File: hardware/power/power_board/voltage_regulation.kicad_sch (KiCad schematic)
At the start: 14 parts, among them U601 TLV76733DRVx, U602 TLV76750DRVx

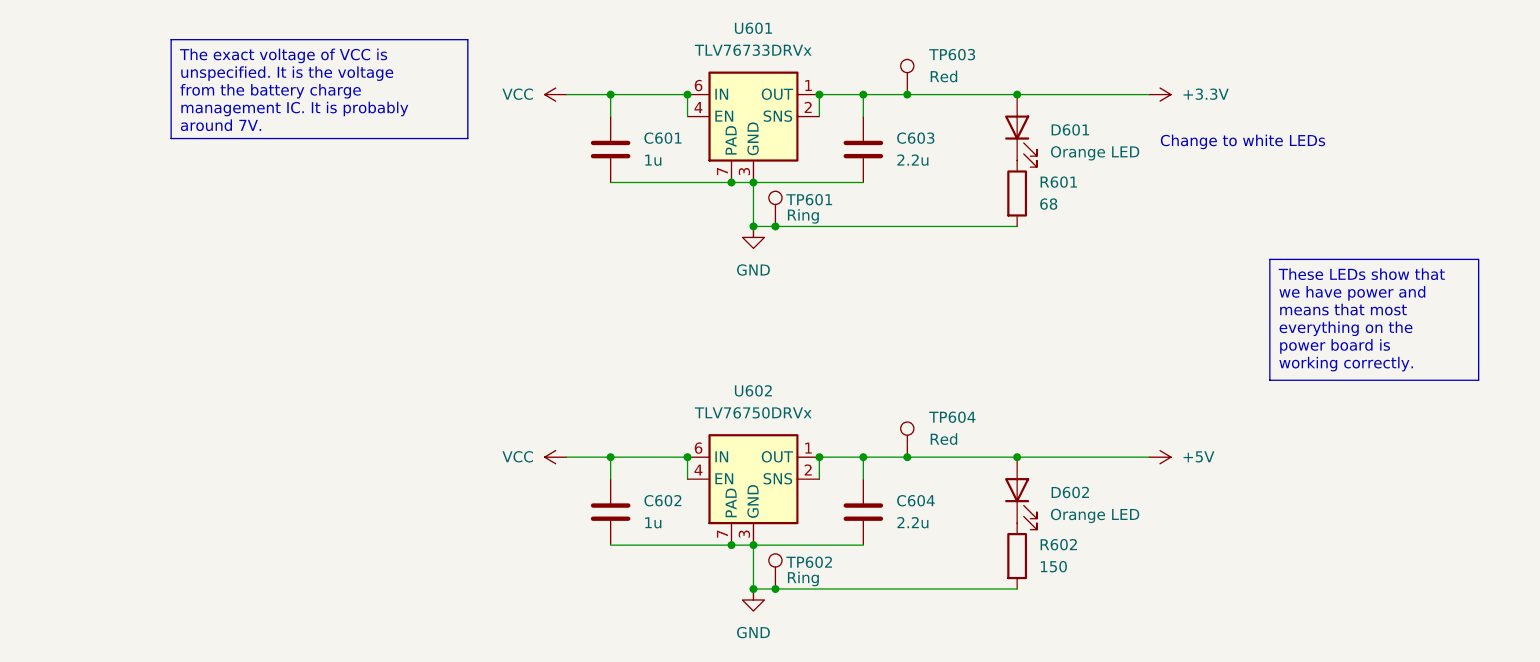
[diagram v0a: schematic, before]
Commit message: Changed interconnect from battery to power board to use the 10-pin Pico-Lock receptacle and cable.
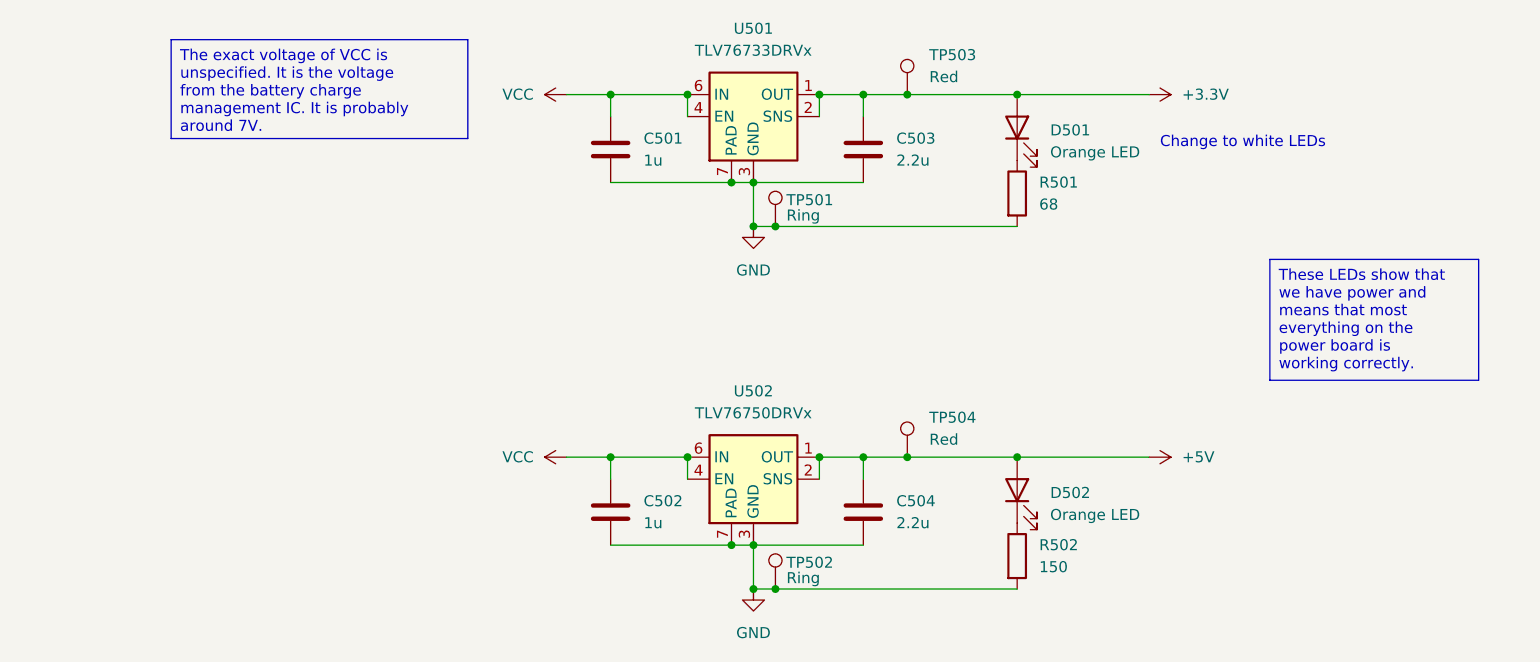
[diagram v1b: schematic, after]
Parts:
- renumbered C601 to C501, C602 to C502, C603 to C503, C604 to C504, D601 to D501, D602 to D502, R601 to R501, R602 to R502, TP601 to TP501, TP602 to TP502, TP603 to TP503, TP604 to TP504, U601 to U501, U602 to U502

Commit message: Checkpointing work on laying out the power board
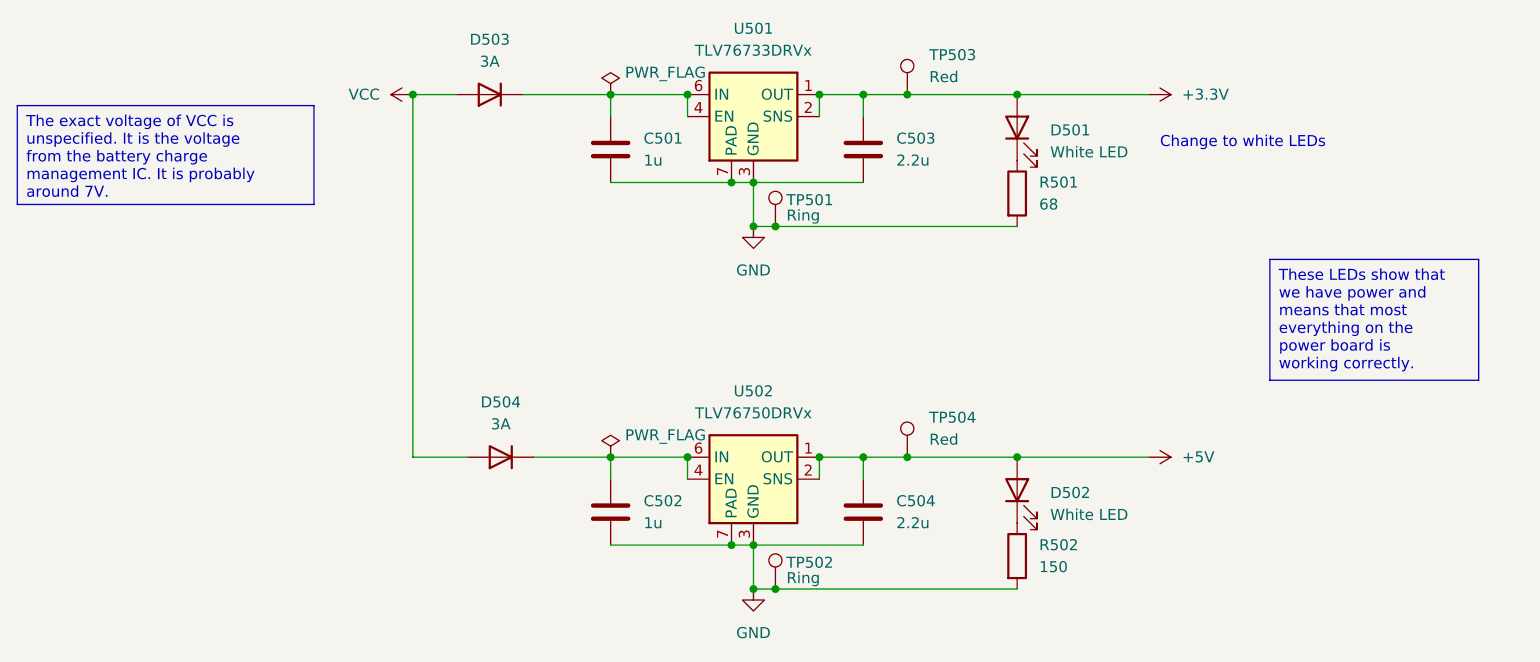
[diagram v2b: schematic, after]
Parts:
- added D503, D504: 3A, Diode_THT:D_DO-15_P2.54mm_Vertical_KathodeUp, symbol Diode:1N4001
- D501, D502: value Orange LED -> White LED; footprint LED_SMD:LED_1210_3225Metric -> LED_SMD:LED_1206_3216Metric; MPN C284943 -> C575513; Manufacturer Part Number LTST-C930KFKT -> LTW-C230DS
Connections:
- net VCC: now also D503.2 (A), D504.2 (A); no longer C501.1, C502.1, U501.4 (EN), U501.6 (IN), U502.4 (EN), U502.6 (IN)
- new net: C501.1, D503.1 (K), U501.4 (EN), U501.6 (IN)
- new net: C502.1, D504.1 (K), U502.4 (EN), U502.6 (IN)

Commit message: Checkpointing work
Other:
- note removed: "Change to white LEDs"
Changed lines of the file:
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@@
     (stroke (width 0) (type default))
   )
-  (text_box "These LEDs show that we have power and means that most everything on the power board is working correctly."
-    (at 185.42 77.47 0) (size 24.13 13.97)
+  (text_box "These LEDs show that we have power and means that most everything on the power board is working correctly.\n\nThey also illuminate any translucent logos on the chassis.\n\nThey also consume a large amount of power as designed."
+    (at 187.96 64.77 0) (size 24.13 31.75)
     (stroke (width 0) (type default))
     (fill (type none))
     (effects (font (size 1.27 1.27)) (justify left top))
   )
-  (text_box "The exact voltage of VCC is unspecified. It is the voltage from the battery charge management IC. It is probably around 7V."
+  (text_box "The exact voltage of VCC is unspecified and varies over time. It is the voltage from the battery charge management IC. It is probably around 7V."
     (at 40.64 59.69 0) (size 34.29 11.43)
     (stroke (width 0) (type default))
@@
     (effects (font (size 1.27 1.27)) (justify left top))
   )
-  (text "Change to white LEDs" (at 172.72 64.77 0)
-    (effects (font (size 1.27 1.27)) (justify left bottom))
-  )
   (symbol (lib_id "Connector:TestPoint") (at 128.27 73.66 0) (unit 1)

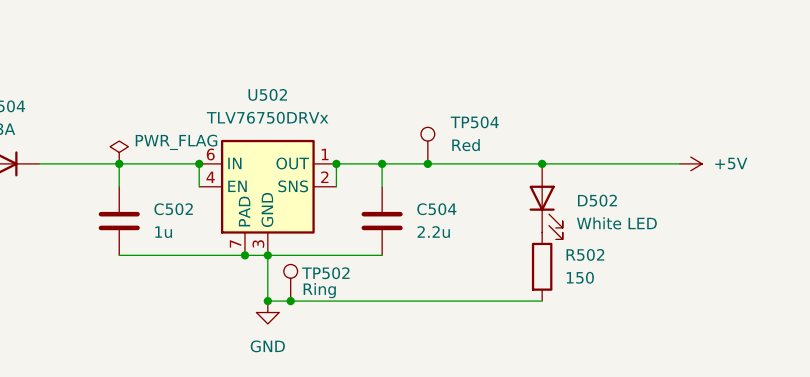
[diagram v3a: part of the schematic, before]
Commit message: Placed all parts on power board PCB
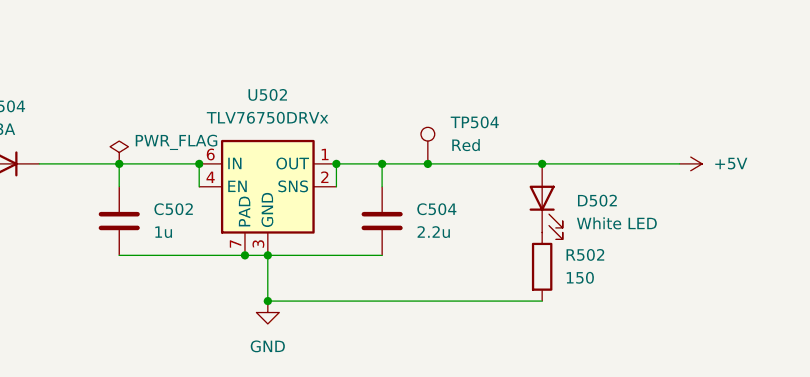
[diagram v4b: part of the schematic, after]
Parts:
- removed TP502: Ring, TestPoint:TestPoint_Keystone_5019_Minature, symbol Connector:TestPoint
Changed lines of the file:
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@@
 (kicad_sch (version 20230121) (generator eeschema)
   (paper "USLetter")
-  (junction (at 128.27 115.57) (diameter 0) (color 0 0 0 0)
-  )
   (junction (at 156.21 58.42) (diameter 0) (color 0 0 0 0)
   )
@@
     (stroke (width 0) (type default))
   )
-  (wire (pts (xy 128.27 115.57) (xy 156.21 115.57))
-    (stroke (width 0) (type default))
-  )
   (wire (pts (xy 118.11 100.33) (xy 118.11 102.87))
     (stroke (width 0) (type default))
@@
     (stroke (width 0) (type default))
   )
-  (wire (pts (xy 125.73 115.57) (xy 128.27 115.57))
+  (wire (pts (xy 125.73 115.57) (xy 156.21 115.57))
     (stroke (width 0) (type default))
   )
@@
         )
       )
-    )
-  )
-  (symbol (lib_id "Connector:TestPoint") (at 128.27 115.57 0) (unit 1)
-    (in_bom yes) (on_board yes) (dnp no)
-    (property "Reference" "TP502" (at 129.54 112.522 0)
-      (effects (font (size 1.27 1.27)) (justify left))
-    )
-    (property "Value" "Ring" (at 129.54 114.3 0)
-      (effects (font (size 1.27 1.27)) (justify left))
-    )
-    (property "Footprint" "TestPoint:TestPoint_Keystone_5019_Minature" (at 133.35 115.57 0)
-      (effects (font (size 1.27 1.27)) hide)
-    )
-    (property "Datasheet" "~" (at 133.35 115.57 0)
-      (effects (font (size 1.27 1.27)) hide)
-    )
-    (property "MPN" "C238131" (at 128.27 115.57 0)
-      (effects (font (size 1.27 1.27)) hide)
-    )
-    (property "Manufacturer" "Keystone" (at 128.27 115.57 0)
-      (effects (font (size 1.27 1.27)) hide)
-    )
-    (property "Manufacturer Part Number" "5019" (at 128.27 115.57 0)
-      (effects (font (size 1.27 1.27)) hide)
-    )
-    (property "Active" "Y" (at 128.27 115.57 0)
-      (effects (font (size 1.27 1.27)) hide)
-    )
-    (property "Purpose" "" (at 128.27 115.57 0)
-      (effects (font (size 1.27 1.27)) hide)
-    )
-    (pin "1")
-    (instances
-      (project "power_board"
-        (path "/d7fbba2e-84c5-4e09-9d36-52dae726d12d/8db3683c-cea4-47e4-9629-920cdb131786"
-          (reference "TP502") (unit 1)
-        )
-      )
